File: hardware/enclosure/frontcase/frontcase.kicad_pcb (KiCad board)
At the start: 2 copper layers, 42.5 x 23 mm, 1 part

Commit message: serial enclosure
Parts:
- moved REF** 1.41 mm to (144.0, 96.0)
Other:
- board size 42.5 x 23 mm -> 63.5 x 30 mm
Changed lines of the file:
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@@
   (net 0 "")
   (footprint "ps2usb:frontpanel" (layer "F.Cu")
-    (at 145 97)
+    (at 144 96)
     (attr through_hole)
     (fp_text reference "REF**" (at 0 -0.5 unlocked) (layer "F.SilkS") hide
@@
       (effects (font (size 1 1) (thickness 0.15)))
     )
-    (fp_line (start 21.25 7.5) (end 21.25 -7.5) (layer "Edge.Cuts") (width 0.12))
-    (fp_line (start 17.25 11.5) (end -17.25 11.5) (layer "Edge.Cuts") (width 0.12))
-    (fp_line (start -21.25 7.5) (end -21.25 -7.5) (layer "Edge.Cuts") (width 0.12))
-    (fp_line (start -17.25 -11.5) (end 17.25 -11.5) (layer "Edge.Cuts") (width 0.12))
-    (fp_arc (start -21.25 -7.5) (mid -20.078427 -10.328427) (end -17.25 -11.5) (layer "Edge.Cuts") (width 0.12))
-    (fp_arc (start 17.25 -11.5) (mid 20.078427 -10.328427) (end 21.25 -7.5) (layer "Edge.Cuts") (width 0.12))
-    (fp_arc (start 21.25 7.5) (mid 20.078427 10.328427) (end 17.25 11.5) (layer "Edge.Cuts") (width 0.12))
-    (fp_arc (start -17.25 11.5) (mid -20.078427 10.328427) (end -21.25 7.5) (layer "Edge.Cuts") (width 0.12))
-    (pad "" np_thru_hole circle (at 8.5 0) (size 13 13) (drill 13) (layers F&B.Cu *.Mask))
-    (pad "" np_thru_hole circle (at 17.8 0) (size 3.5 3.5) (drill 3.5) (layers F&B.Cu *.Mask)
-      (clearance 1))
-    (pad "" np_thru_hole circle (at -17.8 0) (size 3.5 3.5) (drill 3.5) (layers F&B.Cu *.Mask)
-      (clearance 1))
-    (pad "" np_thru_hole circle (at -8.5 0) (size 13 13) (drill 13) (layers F&B.Cu *.Mask))
+    (fp_line (start -31.75 13) (end -31.75 -13) (layer "Edge.Cuts") (width 0.12))
+    (fp_line (start 29.75 15) (end -29.75 15) (layer "Edge.Cuts") (width 0.12))
+    (fp_line (start 31.75 13) (end 31.75 -13) (layer "Edge.Cuts") (width 0.12))
+    (fp_line (start -29.75 -15) (end 29.75 -15) (layer "Edge.Cuts") (width 0.12))
+    (fp_arc (start -31.75 -13) (mid -31.164214 -14.414214) (end -29.75 -15) (layer "Edge.Cuts") (width 0.12))
+    (fp_arc (start 29.75 -15) (mid 31.164214 -14.414214) (end 31.75 -13) (layer "Edge.Cuts") (width 0.12))
+    (fp_arc (start -29.75 15) (mid -31.164214 14.414214) (end -31.75 13) (layer "Edge.Cuts") (width 0.12))
+    (fp_arc (start 31.75 13) (mid 31.164214 14.414214) (end 29.75 15) (layer "Edge.Cuts") (width 0.12))
+    (pad "" np_thru_hole circle (at 0 2.95) (size 4 4) (drill 4) (layers F&B.Cu *.Mask))
+    (pad "1" thru_hole circle (at -25.75 11.5) (size 5 5) (drill 3.5) (layers *.Cu *.Mask))
+    (pad "1" thru_hole circle (at 25.75 -10) (size 5 5) (drill 3.5) (layers *.Cu *.Mask))
+    (pad "1" thru_hole circle (at -25.75 -10) (size 5 5) (drill 3.5) (layers *.Cu *.Mask))
+    (pad "1" thru_hole circle (at 25.75 11.5) (size 5 5) (drill 3.5) (layers *.Cu *.Mask))
+    (pad "2" thru_hole circle (at -17.5 0.6) (size 13 13) (drill 13) (layers *.Cu *.Mask))
+    (pad "2" thru_hole circle (at 17.5 0.6) (size 13 13) (drill 13) (layers *.Cu *.Mask))
   )
   (gr_line (start 135.393669 106.96999) (end 135.388079 106.969565) (layer "F.SilkS") (width 0.333132))
@@
   (gr_line (start 137.674673 88.971407) (end 137.670679 88.974866) (layer "F.SilkS") (width 0.333132))
   (gr_line (start 153.597551 89.745105) (end 153.549106 89.748766) (layer "F.SilkS") (width 0.32))
-  (gr_rect (start 123.75 85.5) (end 166.25 108.5) (layer "B.Mask") (width 0.15) (fill solid))
+  (gr_rect (start 111.75 80.5) (end 176.25 111.5) (layer "B.Mask") (width 0.15) (fill solid))
   (gr_poly
     (pts
@@
     (polygon
       (pts
-        (xy 166.25 108.5)
-        (xy 123.75 108.5)
-        (xy 123.75 85.5)
-        (xy 166.25 85.5)
+        (xy 176.25 111.5)
+        (xy 111.75 111.5)
+        (xy 111.75 80.5)
+        (xy 176.25 80.5)
       )
     )
@@
     (polygon
       (pts
-        (xy 166.245386 108.498846)
-        (xy 123.745386 108.498846)
-        (xy 123.745386 85.498846)
-        (xy 166.245386 85.498846)
+        (xy 176.245386 111.498846)
+        (xy 111.745386 111.498846)
+        (xy 111.745386 80.498846)
+        (xy 176.245386 80.498846)
       )
     )

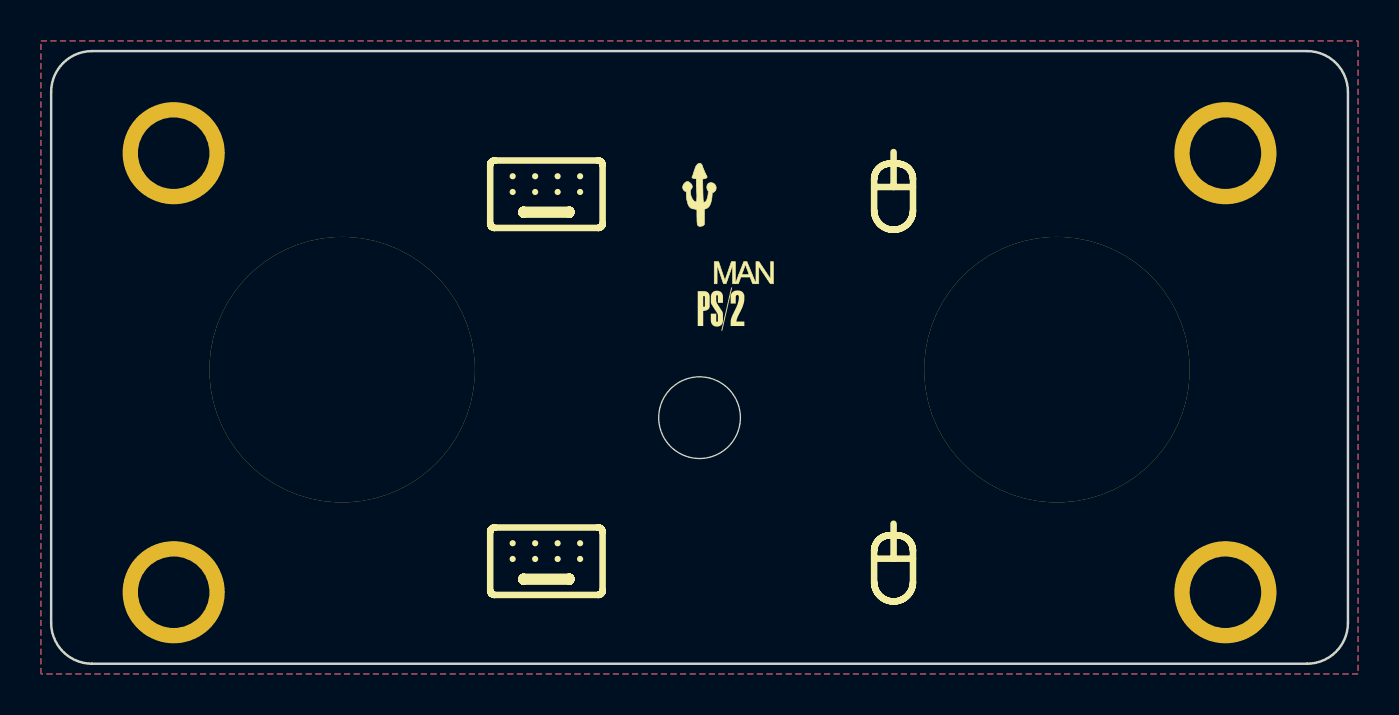
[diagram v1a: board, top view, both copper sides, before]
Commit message: Serial version board/enclosure rework
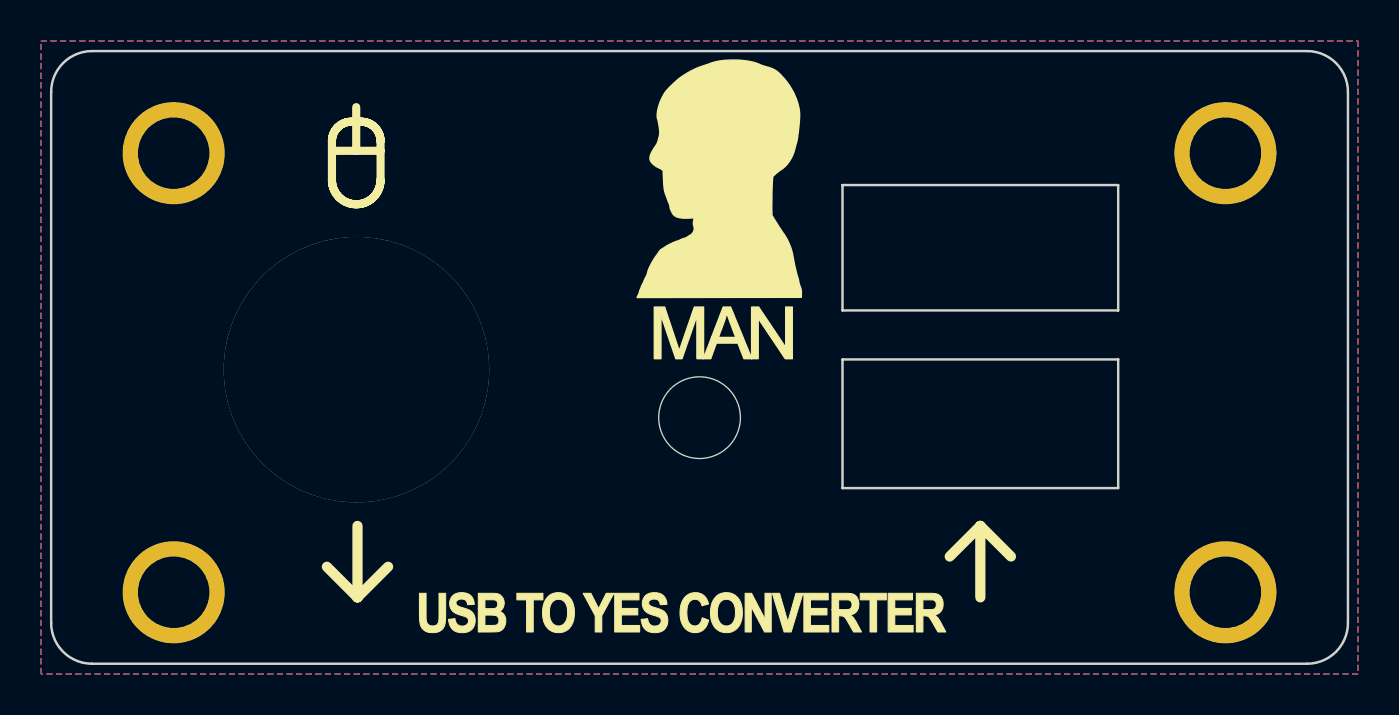
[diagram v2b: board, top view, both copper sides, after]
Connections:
- REF** pad 1: (no net) -> GND
- REF** pad 2: (no net) -> GND
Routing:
- added copper zone on B.Cu, net GND
- added copper zone on F.Cu, net GND
- removed copper zone on F.Cu, net (none)
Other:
- outline, holes or cut-outs redrawn

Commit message: Finished serial enclosure
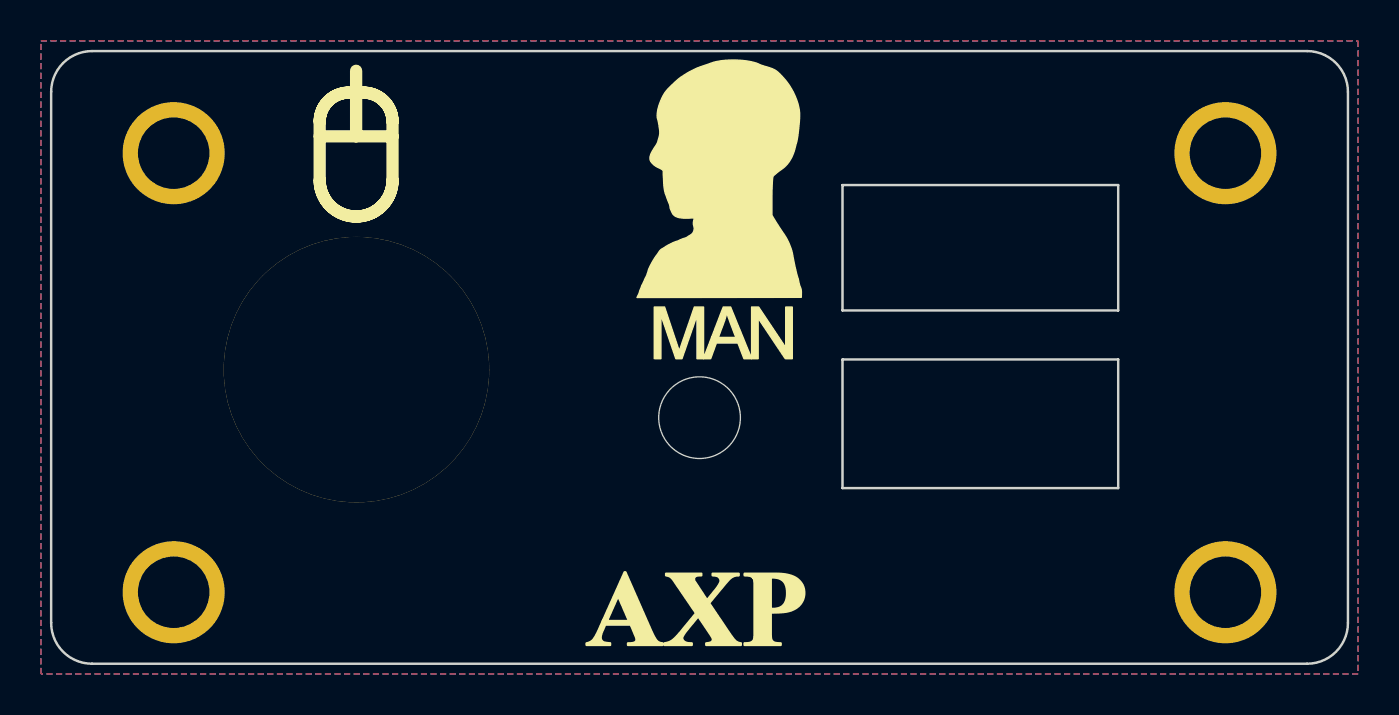
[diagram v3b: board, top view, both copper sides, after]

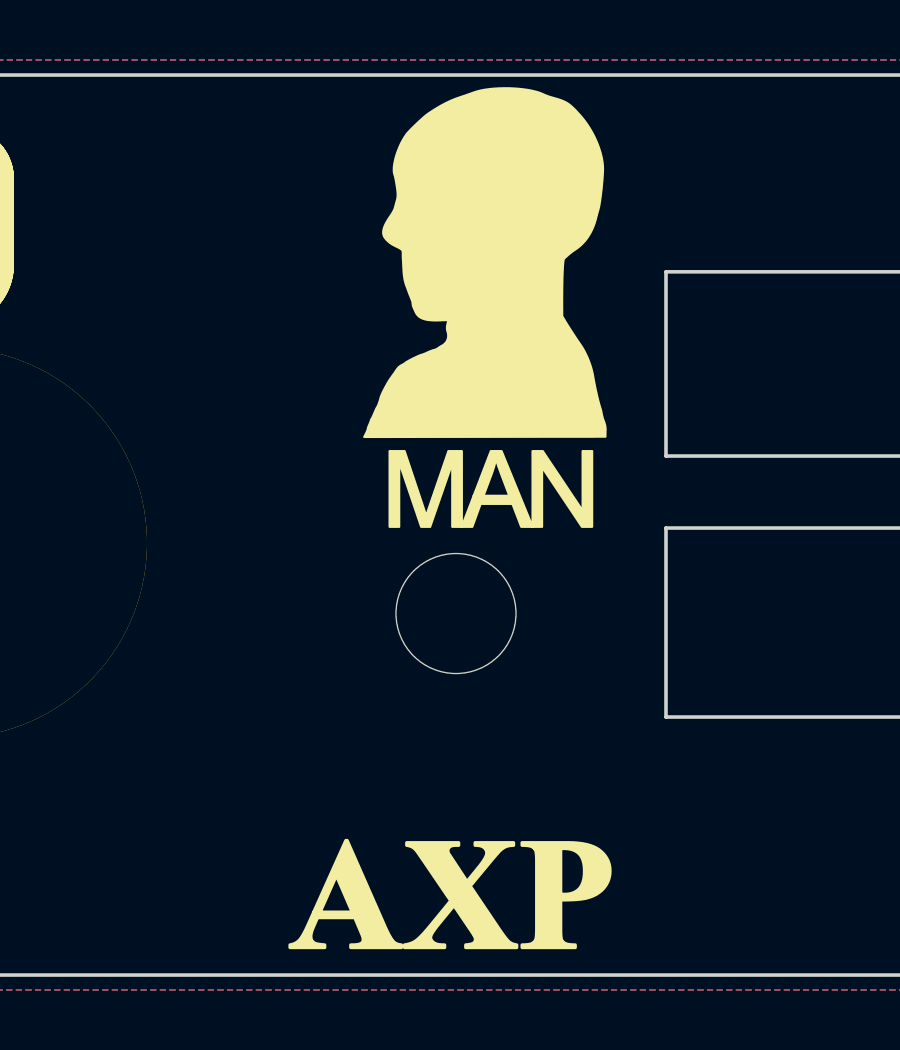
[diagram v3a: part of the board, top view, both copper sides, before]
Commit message: button position change
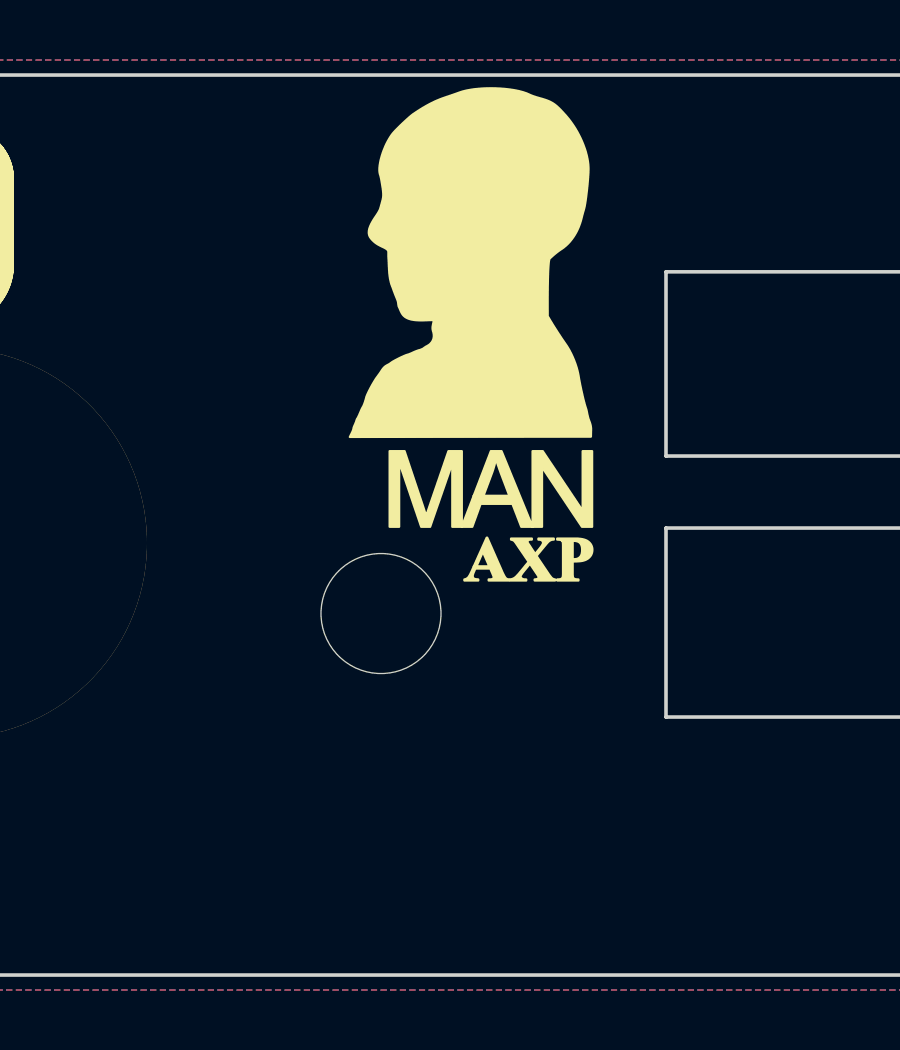
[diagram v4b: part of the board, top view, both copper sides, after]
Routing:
- removed copper zone on B.Cu, net (none)
